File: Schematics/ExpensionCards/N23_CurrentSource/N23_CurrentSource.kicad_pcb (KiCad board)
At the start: 2 copper layers, 100 x 64 mm, 66 parts

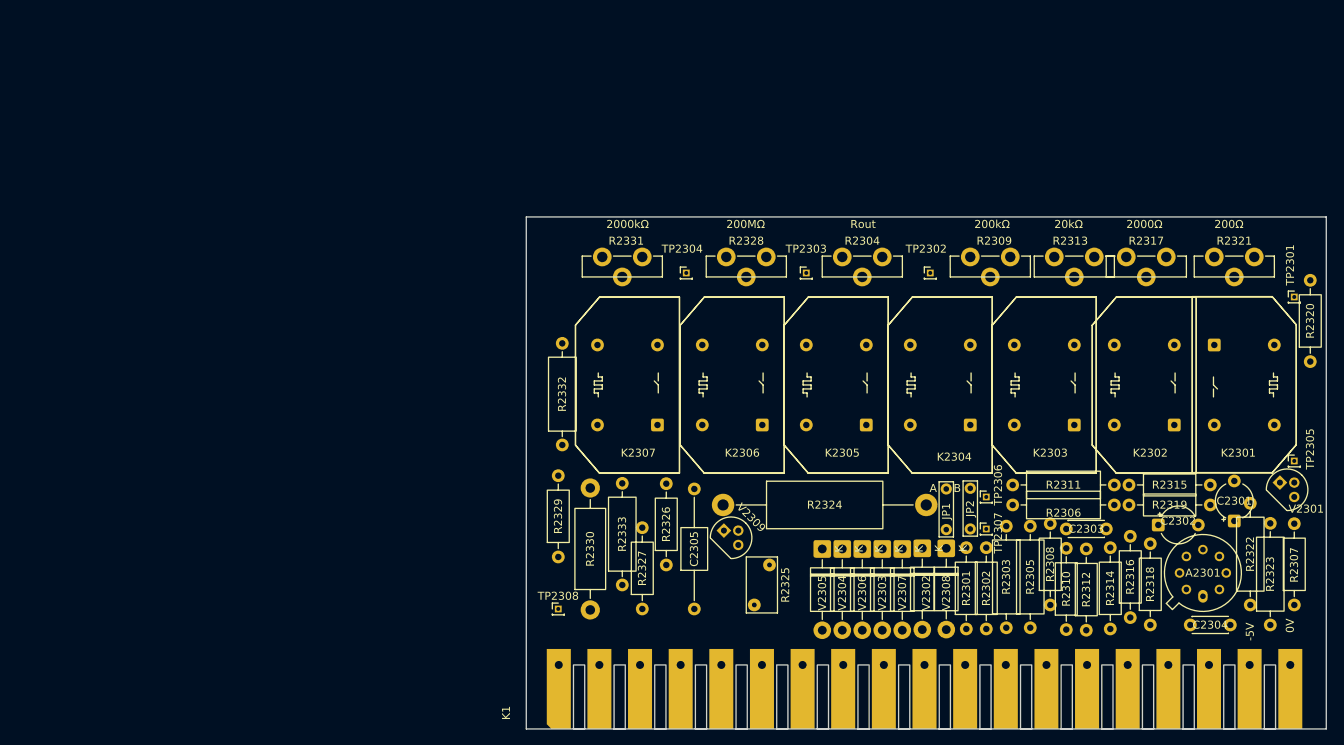
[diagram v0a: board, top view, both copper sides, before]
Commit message: Reworked N20/N21
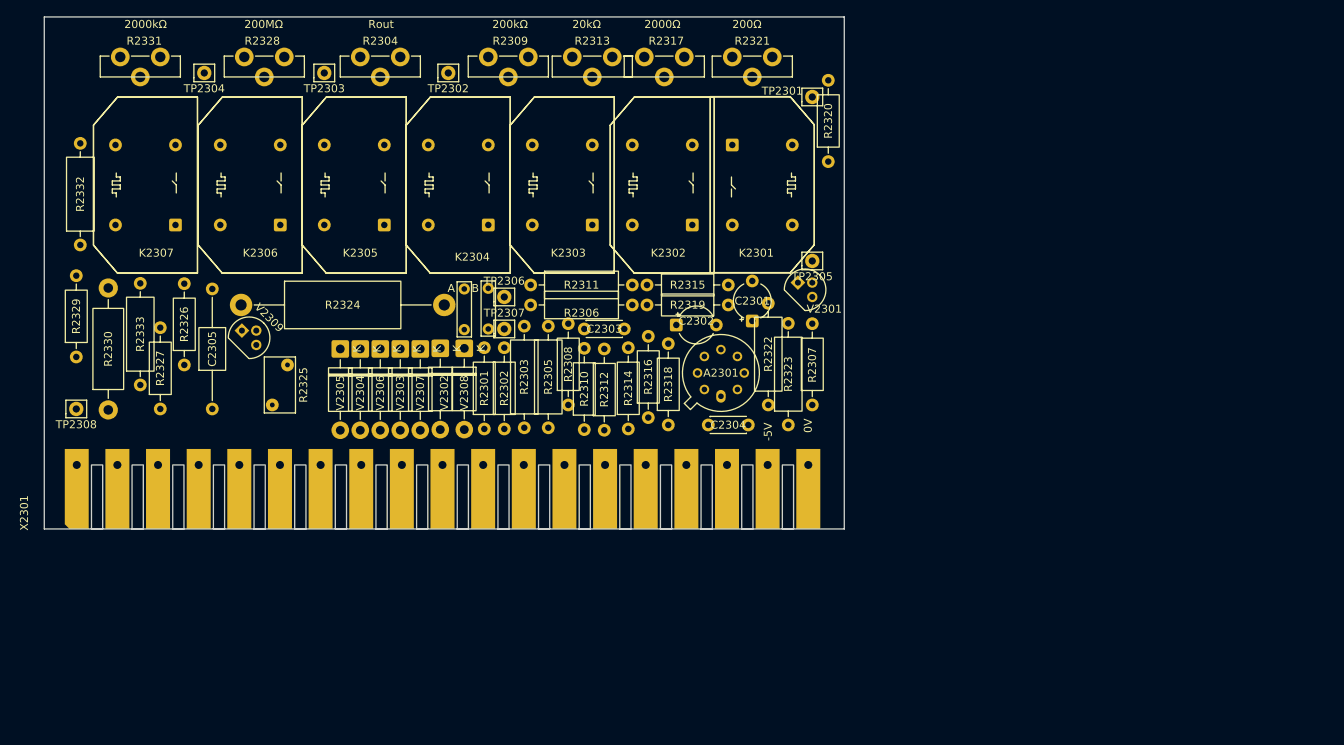
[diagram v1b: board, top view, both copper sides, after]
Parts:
- R2304, R2309, R2313, R2317, R2321, R2328, R2331: footprint PM2528:Potentiometer horizontal ceramic -> PM2528:Trimmer vertical
- TP2301, TP2302, TP2303, TP2304, TP2305, TP2306, TP2307, TP2308: footprint Connector_PinHeader_1.00mm:PinHeader_1x01_P1.00mm_Vertical -> Connector_Pin:Pin_D0.9mm_L10.0mm_W2.4mm_FlatFork
- moved A2301 65.2 mm to (184.3, 115.9)
- moved C2301 65.2 mm to (188.2, 106.5)
- moved C2302 65.2 mm to (178.8, 107.0)
- moved C2303 65.2 mm to (167.2, 107.5)
- moved C2304 65.2 mm to (182.8, 119.5)
- moved C2305 65.2 mm to (120.8, 117.5)
- moved JP2301 65.2 mm to (152.2, 102.5)
- moved JP2302 65.2 mm to (155.2, 107.5)
- moved K2301 65.2 mm to (185.7, 84.5)
- moved K2302 65.2 mm to (180.8, 94.5)
- moved K2303 65.2 mm to (168.3, 94.5)
- moved K2304 65.2 mm to (155.3, 94.5)
- moved K2305 65.2 mm to (142.3, 94.5)
- moved K2306 65.2 mm to (129.3, 94.5)
- moved K2307 65.2 mm to (116.2, 94.5)
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- renumbered JP1 to JP2301, JP2 to JP2302, K1 to X2301
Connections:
- A2301 pad 3: /_N2157 -> Net-(A2301-+)
- R2305 pad 2: /_N2157 -> Net-(A2301-+)
- R2308 pad 1: /_N2157 -> Net-(A2301-+)
- R2309 pad 1: /_N2157 -> Net-(R2308-Pad2)
- R2309 pad 3: Net-(R2308-Pad2) -> Net-(A2301-+)
- R2313 pad 1: Net-(R2311-Pad2) -> Net-(R2312-Pad2)
- R2313 pad 3: Net-(R2312-Pad2) -> Net-(R2311-Pad2)
- R2317 pad 1: Net-(R2315-Pad2) -> Net-(R2316-Pad2)
- R2317 pad 3: Net-(R2316-Pad2) -> Net-(R2315-Pad2)
- R2321 pad 1: Net-(R2319-Pad2) -> Net-(R2320-Pad2)
- R2321 pad 3: Net-(R2320-Pad2) -> Net-(R2319-Pad2)

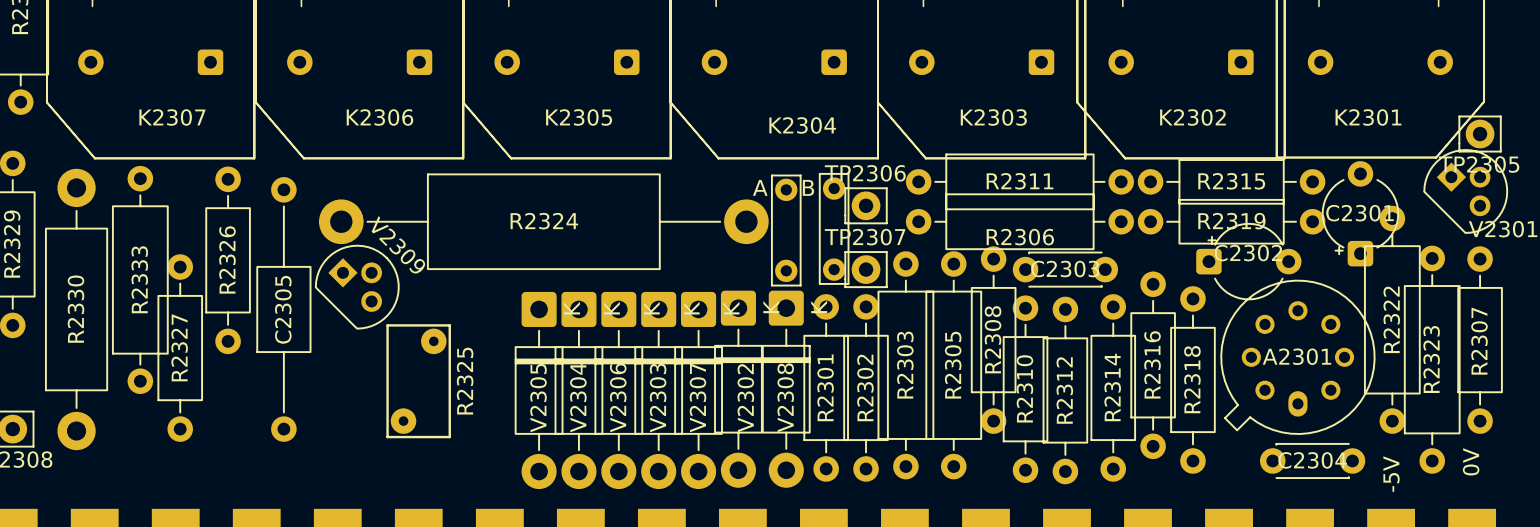
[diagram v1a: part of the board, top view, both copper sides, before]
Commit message: Small modifications, more disassembly
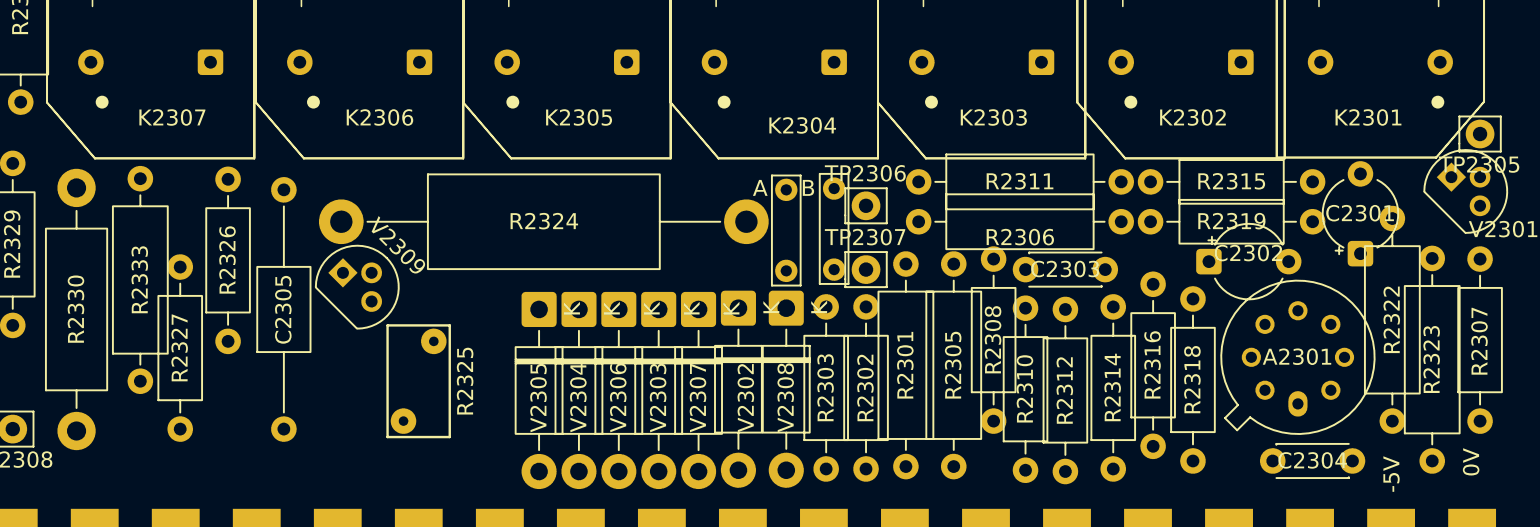
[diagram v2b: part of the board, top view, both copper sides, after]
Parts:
- JP2301: value A -> B
- JP2302: value B -> A
- R2301: renamed from R2303; value 200k -> 487
- R2303: renamed from R2301; value 487 -> 200k
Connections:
- net /N2157 renamed /VrefZero
- R2326 pad 1: Net-(K2306-Pad5) -> Net-(R2326-Pad1)
- R2326 pad 2: Net-(R2326-Pad2) -> Net-(K2306-Pad5)
- R2327 pad 1: Net-(R2326-Pad2) -> GND1
- R2327 pad 2: GND1 -> Net-(R2326-Pad1)
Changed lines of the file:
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@@
 	(title_block
 		(title "Philips PM2528 - N23 (Current Source)")
-		(date "2025-08-06")
+		(date "2025-08-10")
 		(rev "1.0")
 		(company "D. Kupers")
@@
 	(net 20 "/REL2306")
 	(net 21 "/REL2307")
-	(net 22 "/N2157")
+	(net 22 "/VrefZero")
 	(net 23 "/REL2303")
 	(net 24 "unconnected-(X2301--5V-Pad2)")
@@
 	(net 48 "Net-(R2322-Pad1)")
 	(net 49 "Net-(R2324-Pad2)")
-	(net 50 "Net-(R2326-Pad2)")
+	(net 50 "Net-(R2326-Pad1)")
 	(net 51 "Net-(R2328-Pad2)")
 	(net 52 "Net-(R2329-Pad2)")
@@
 		(descr "Resistor, Axial_DIN0309 series, Axial, Horizontal, pin pitch=12.7mm, 0.5W = 1/2W, length*diameter=9*3.2mm^2, http://cdn-reichelt.de/documents/datenblatt/B400/1_4W%23YAG.pdf")
 		(tags "Resistor Axial_DIN0309 series Axial Horizontal pin pitch 12.7mm 0.5W = 1/2W length 9mm diameter 3.2mm")
-		(property "Reference" "R2303"
+		(property "Reference" "R2301"
 			(at 6.35 0 90)
 			(layer "F.SilkS")
@@
 			)
 		)
-		(property "Value" "200k"
+		(property "Value" "487"
 			(at 6.35 2.72 90)
 			(layer "F.Fab")
@@
 			(layers "*.Cu" "*.Mask")
 			(remove_unused_layers no)
-			(net 22 "/N2157")
+			(net 22 "/VrefZero")
 			(pintype "passive")
 		)
@@
 			)
 		)
-		(property "Value" "A"
+		(property "Value" "B"
 			(at 1 -1.7 90)
 			(layer "F.Fab")
@@
 			(layers "*.Cu" "*.Mask")
 			(remove_unused_layers no)
-			(net 22 "/N2157")
+			(net 22 "/VrefZero")
 			(pinfunction "1")
 			(pintype "passive")
@@
 			(layers "*.Cu" "*.Mask")
 			(remove_unused_layers no)
-			(net 50 "Net-(R2326-Pad2)")
+			(net 28 "GND1")
 			(pintype "passive")
 		)
@@
 			(layers "*.Cu" "*.Mask")
 			(remove_unused_layers no)
-			(net 28 "GND1")
+			(net 50 "Net-(R2326-Pad1)")
 			(pintype "passive")
 		)
@@
 			(layers "*.Cu" "*.Mask")
 			(remove_unused_layers no)
-			(net 22 "/N2157")
+			(net 22 "/VrefZero")
 			(pinfunction "1")
 			(pintype "passive")
@@
 			(layers "*.Cu" "*.Mask")
 			(remove_unused_layers no)
-			(net 22 "/N2157")
+			(net 22 "/VrefZero")
 			(pinfunction "2")
 			(pintype "passive")
@@
 			)
 		)
-		(property "Value" "B"
+		(property "Value" "A"
 			(at 1 -1.7 90)
 			(layer "F.Fab")
@@
 		(descr "Resistor, Axial_DIN0207 series, Axial, Horizontal, pin pitch=10.16mm, 0.25W = 1/4W, length*diameter=6.3*2.5mm^2, http://cdn-reichelt.de/documents/datenblatt/B400/1_4W%23YAG.pdf")
 		(tags "Resistor Axial_DIN0207 series Axial Horizontal pin pitch 10.16mm 0.25W = 1/4W length 6.3mm diameter 2.5mm")
-		(property "Reference" "R2301"
+		(property "Reference" "R2303"
 			(at 5.08 0 90)
 			(layer "F.SilkS")
@@
 			)
 		)
-		(property "Value" "487"
+		(property "Value" "200k"
 			(at 5.08 2.37 90)
 			(layer "F.Fab")
@@
 			(layers "*.Cu" "*.Mask")
 			(remove_unused_layers no)
-			(net 35 "Net-(K2306-Pad5)")
+			(net 50 "Net-(R2326-Pad1)")
 			(pintype "passive")
 		)
@@
 			(layers "*.Cu" "*.Mask")
 			(remove_unused_layers no)
-			(net 50 "Net-(R2326-Pad2)")
+			(net 35 "Net-(K2306-Pad5)")
 			(pintype "passive")
 		)
@@
 		)
 	)
+	(gr_circle
+		(center 193.103553 97)
+		(end 193.353553 97.25)
+		(stroke
+			(width 0.1)
+			(type solid)
+		)
+		(fill yes)
+		(layer "F.SilkS")
+	)
+	(gr_circle
+		(center 148.353553 97)
+		(end 148.603553 97.25)
+		(stroke
+			(width 0.1)
+			(type solid)
+		)
+		(fill yes)
+		(layer "F.SilkS")
+	)
+	(gr_circle
+		(center 109.353553 97)
+		(end 109.603553 97.25)
+		(stroke
+			(width 0.1)
+			(type solid)
+		)
+		(fill yes)
+		(layer "F.SilkS")
+	)
+	(gr_circle
+		(center 122.603553 97)
+		(end 122.853553 97.25)
+		(stroke
+			(width 0.1)
+			(type solid)
+		)
+		(fill yes)
+		(layer "F.SilkS")
+	)
+	(gr_circle
+		(center 161.353553 97)
+		(end 161.603553 97.25)
+		(stroke
+			(width 0.1)
+			(type solid)
+		)
+		(fill yes)
+		(layer "F.SilkS")
+	)
+	(gr_circle
+		(center 173.853553 97)
+		(end 174.103553 97.25)
+		(stroke
+			(width 0.1)
+			(type solid)
+		)
+		(fill yes)
+		(layer "F.SilkS")
+	)
+	(gr_circle
+		(center 135.103553 97)
+		(end 135.353553 97.25)
+		(stroke
+			(width 0.1)
+			(type solid)
+		)
+		(fill yes)
+		(layer "F.SilkS")
+	)
 	(gr_rect
